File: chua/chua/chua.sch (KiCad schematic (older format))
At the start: 31 parts, among them J1 AudioJack2, J2 Conn_Coaxial, J3 Conn_01x02_Male, J4 Conn_Coaxial, K1 CONN_3, P1 CONN_1, P2 CONN_1, Q1 2N7000, U1 LM741, U2 LM741, U3 LM741

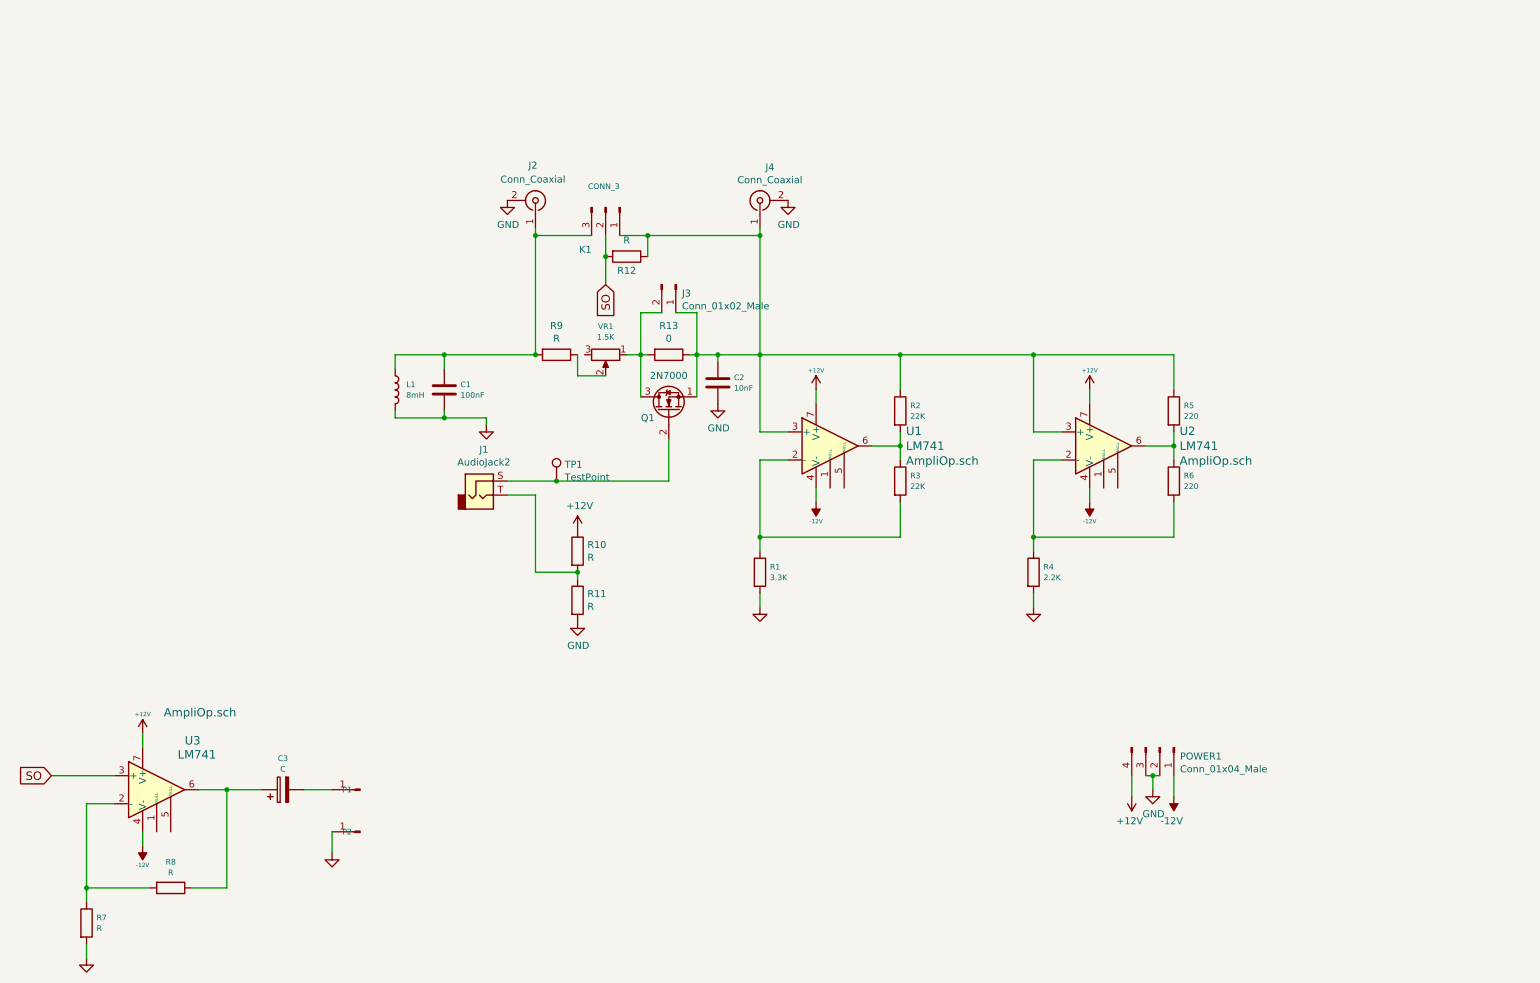
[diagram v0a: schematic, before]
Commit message: Added new power connector
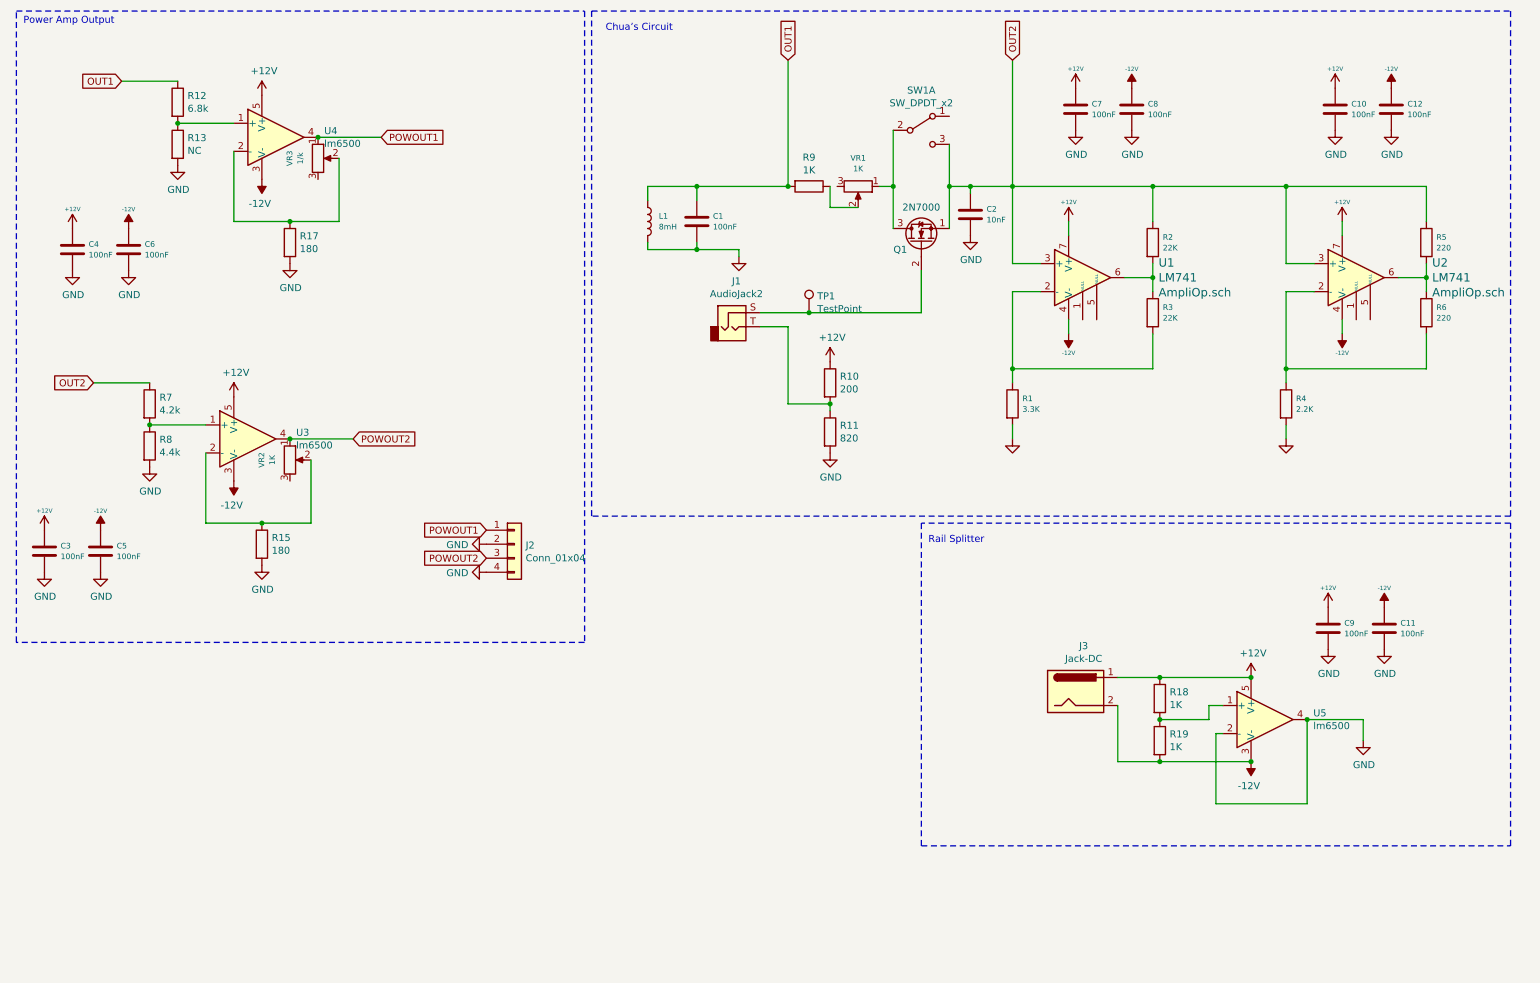
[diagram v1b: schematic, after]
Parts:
- removed C3: C, Capacitors_THT:CP_Radial_D5.0mm_P2.50mm, symbol Device:CP
- removed J2, J4: Conn_Coaxial, Connectors:SMA_THT_Jack_Straight, symbol Connector:Conn_Coaxial
- removed J3: Conn_01x02_Male, Socket_Strips:Socket_Strip_Straight_1x02_Pitch2.54mm, symbol Connector:Conn_01x02_Male
- removed K1: CONN_3, Socket_Strips:Socket_Strip_Straight_1x03_Pitch2.54mm, symbol Connector:Conn_01x03_Male
- removed P1, P2: CONN_1, Socket_Strips:Socket_Strip_Straight_1x01_Pitch2.54mm, symbol Connector:Conn_01x01_Male
- removed POWER1: Conn_01x04_Male, Socket_Strips:Socket_Strip_Straight_1x04_Pitch2.54mm, symbol Connector:Conn_01x04_Male
- removed U3: LM741, Housings_DIP:DIP-8_W7.62mm_LongPads, symbol Amplifier_Operational:LM741
- added C10, C11, C12, C3, C4, C5, C6, C7, C8, C9: 100nF, Capacitor_THT:C_Rect_L4.0mm_W2.5mm_P2.50mm, symbol Device:C
- added J2: Conn_01x04, TerminalBlock_TE-Connectivity:TerminalBlock_TE_282834-4_1x04_P2.54mm_Horizontal, symbol Connector_Generic:Conn_01x04
- added J3: Jack-DC, Connector_BarrelJack:BarrelJack_CUI_PJ-063AH_Horizontal, symbol Connector:Jack-DC
- added R15, R17: 180, Resistor_THT:R_Axial_DIN0207_L6.3mm_D2.5mm_P10.16mm_Horizontal, symbol Device:R
- added R18, R19: 1K, Resistor_THT:R_Axial_DIN0207_L6.3mm_D2.5mm_P10.16mm_Horizontal, symbol Device:R
- added SW1: SW_DPDT_x2, switch:CK_FARN1201430, symbol Switch:SW_DPDT_x2
- added U3, U4, U5: lm6500, Package_TO_SOT_THT:TO-220-5_P3.4x3.7mm_StaggerOdd_Lead3.8mm_Vertical, symbol lm6500:lm6500
- added VR2: 1K, VR_B10K:Potentiometer_WirePads_largePads, symbol Device:R_POT
- added VR3: 1/k, VR_B10K:Potentiometer_WirePads_largePads, symbol Device:R_POT
- R1, R2, R3, R4, R5, R6: footprint Resistors_Universal:Resistor_SMD+THTuniversal_1206_RM10_HandSoldering -> Resistor_THT:R_Axial_DIN0207_L6.3mm_D2.5mm_P10.16mm_Horizontal
- R10: value R -> 200; footprint Resistors_Universal:Resistor_SMD+THTuniversal_1206_RM10_HandSoldering -> Resistor_THT:R_Axial_DIN0207_L6.3mm_D2.5mm_P10.16mm_Horizontal
- R11: value R -> 820; footprint Resistors_Universal:Resistor_SMD+THTuniversal_1206_RM10_HandSoldering -> Resistor_THT:R_Axial_DIN0207_L6.3mm_D2.5mm_P10.16mm_Horizontal
- R12: value R -> 6.8k; footprint Resistors_Universal:Resistor_SMD+THTuniversal_1206_RM10_HandSoldering -> Resistor_THT:R_Axial_DIN0207_L6.3mm_D2.5mm_P10.16mm_Horizontal
- R13: value 0 -> NC; footprint Resistors_Universal:Resistor_SMD+THTuniversal_1206_RM10_HandSoldering -> Resistor_THT:R_Axial_DIN0207_L6.3mm_D2.5mm_P10.16mm_Horizontal
- R7: value R -> 4.2k; footprint Resistors_Universal:Resistor_SMD+THTuniversal_1206_RM10_HandSoldering -> Resistor_THT:R_Axial_DIN0207_L6.3mm_D2.5mm_P10.16mm_Horizontal
- R8: value R -> 4.4k; footprint Resistors_Universal:Resistor_SMD+THTuniversal_1206_RM10_HandSoldering -> Resistor_THT:R_Axial_DIN0207_L6.3mm_D2.5mm_P10.16mm_Horizontal
- R9: value R -> 1K; footprint Resistors_Universal:Resistor_SMD+THTuniversal_1206_RM10_HandSoldering -> Resistor_THT:R_Axial_DIN0207_L6.3mm_D2.5mm_P10.16mm_Horizontal
- VR1: value 1.5K -> 1K; footprint Potentiometers:Potentiometer_WirePads_largePads -> VR_B10K:Potentiometer_WirePads_largePads
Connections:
- net +12V: now also C10.1, C3.1, C4.1, C7.1, C9.1, J3.1, R18.1, U3.5 (V+), U4.5 (V+), U5.5 (V+)
- net -12V: now also C11.1, C12.1, C5.1, C6.1, C8.1, J3.2, R19.2, U3.3 (V-), U4.3 (V-), U5.3 (V-)
- net GND: now also R13.2, R8.2, C10.2, C11.2, C12.2, C3.2, C4.2, C5.2, C6.2, C7.2, C8.2, C9.2, J2.2 (Pin_2), J2.4 (Pin_4), R15.2, R17.2, U5.2 (-), U5.4; no longer R7.2
- net OUT2: now reaches C2.1, Q1.1 (S), R2.1, R5.1, U1.3 (+), U2.3 (+)
- net OUT2: now also R7.1, SW1.3 (C); no longer R12.1, R13.1
- net OUT1: now reaches C1.1, L1.1, R9.2
- net OUT1: now also R12.1
- net at Q1.3 (D), VR1.1: now also SW1.2 (B); no longer R13.2
- net at R8.1: now also R7.2, U3.1 (+)
- net SO: no longer names the net of R12.2
- net SO: now also R13.1, U4.1 (+)
- new net: R15.1, U3.2 (-), VR2.2
- new net: R18.2, R19.1, U5.1 (+)
- new net: R17.1, U4.2 (-), VR3.2
- new net POWOUT1: J2.1 (Pin_1), U4.4, VR3.1
- new net POWOUT2: J2.3 (Pin_3), U3.4, VR2.1
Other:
- note added: "Chua’s Circuit"
- note added: "Power Amp Output"
- note added: "Rail Splitter"
- moved on the sheet: C1, C2, J1, L1, Q1, R1, R10, R11, R2, R3, R4, R5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
